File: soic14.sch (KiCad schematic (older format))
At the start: 2 parts, among them J1 Conn_02x07_Counter_Clockwise, J2 Conn_02x07_Counter_Clockwise

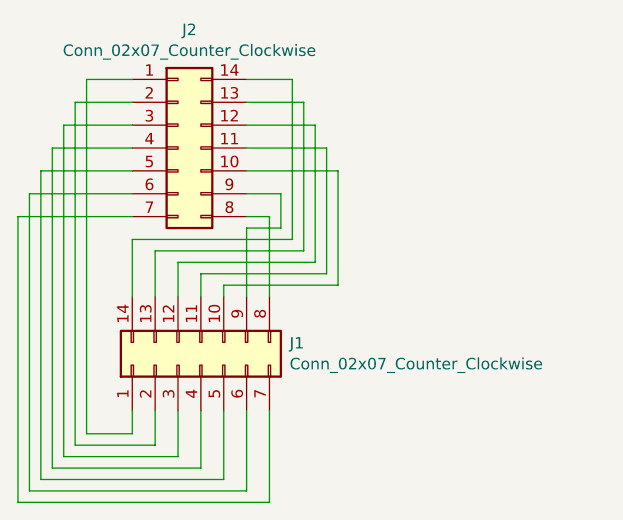
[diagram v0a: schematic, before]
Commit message: version 3 adds capacitor and combs traces
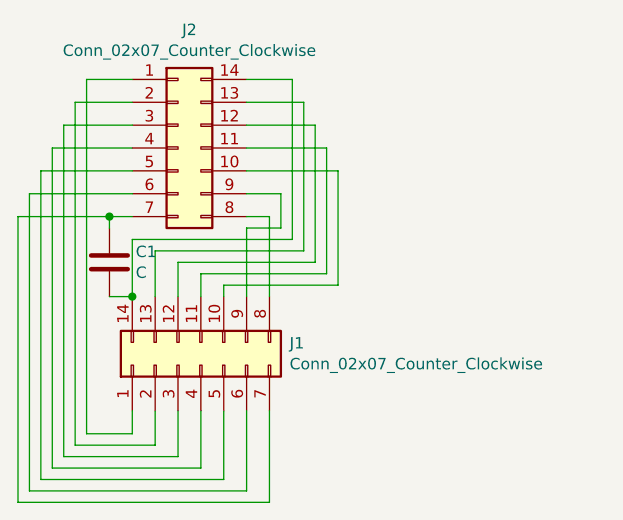
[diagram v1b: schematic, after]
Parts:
- added C1: C, Capacitor_SMD:C_0805_2012Metric_Pad1.15x1.40mm_HandSolder, symbol Device:C
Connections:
- net at J1.14 (Pin_14), J2.14 (Pin_14): now also C1.2
- net at J1.7 (Pin_7), J2.7 (Pin_7): now also C1.1
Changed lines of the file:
@@
 	5250 5550 5250 5200
 Wire Wire Line
-	4750 4350 4250 4350
+	4750 4350 4650 4350
 Wire Wire Line
 	4250 4350 4250 5600
@@
 Wire Wire Line
 	5350 4350 5350 4700
+$Comp
+L Device:C C1
+U 1 1 67B65F50
+P 4650 4550
+F 0 "C1" H 4765 4596 50  0000 L CNN
+F 1 "C" H 4765 4505 50  0000 L CNN
+F 2 "Capacitor_SMD:C_0805_2012Metric_Pad1.15x1.40mm_HandSolder" H 4688 4400 50  0001 C CNN
+F 3 "~" H 4650 4550 50  0001 C CNN
+	1    4650 4550
+	1    0    0    -1
+$EndComp
+Wire Wire Line
+	4650 4400 4650 4350
+Connection ~ 4650 4350
+Wire Wire Line
+	4650 4350 4250 4350
+Wire Wire Line
+	4650 4700 4750 4700
+Connection ~ 4750 4700
 $EndSCHEMATC
